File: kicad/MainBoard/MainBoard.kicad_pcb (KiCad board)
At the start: 2 copper layers, 191.5 x 166.3 mm, 104 parts, among them J1 CHAN1, J10 ACC Port, J11 433TX, J12 VDC INPUT, J13 BAT, J14 TRG1, J15 TRG2, J16 FP-BUTTONS, J17 EXPAN2, J18 OUTPUT_BOARD_POWER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

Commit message: Convert board to Kicad 8
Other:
- net class Default removed

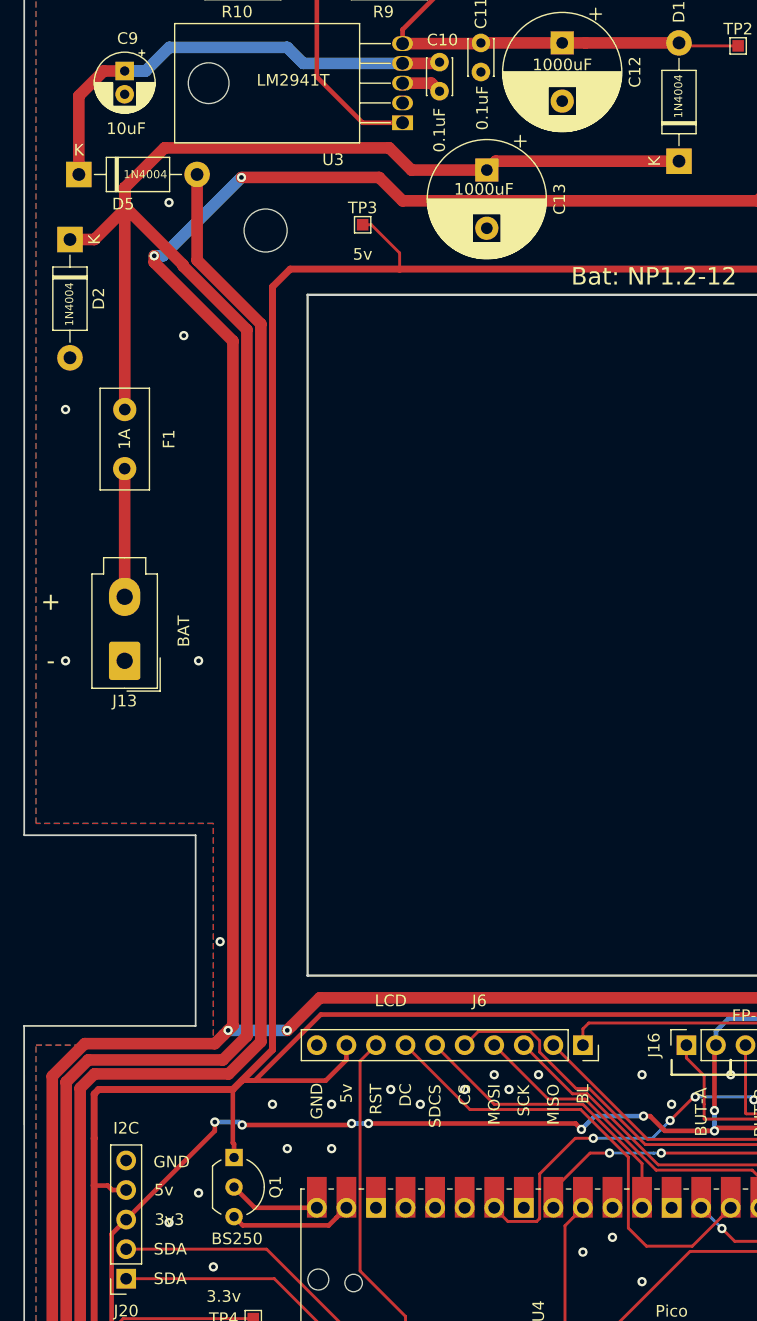
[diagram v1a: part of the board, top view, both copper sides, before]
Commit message: Switch Mainboard Q1, D1, D2, D5 with 1N5819
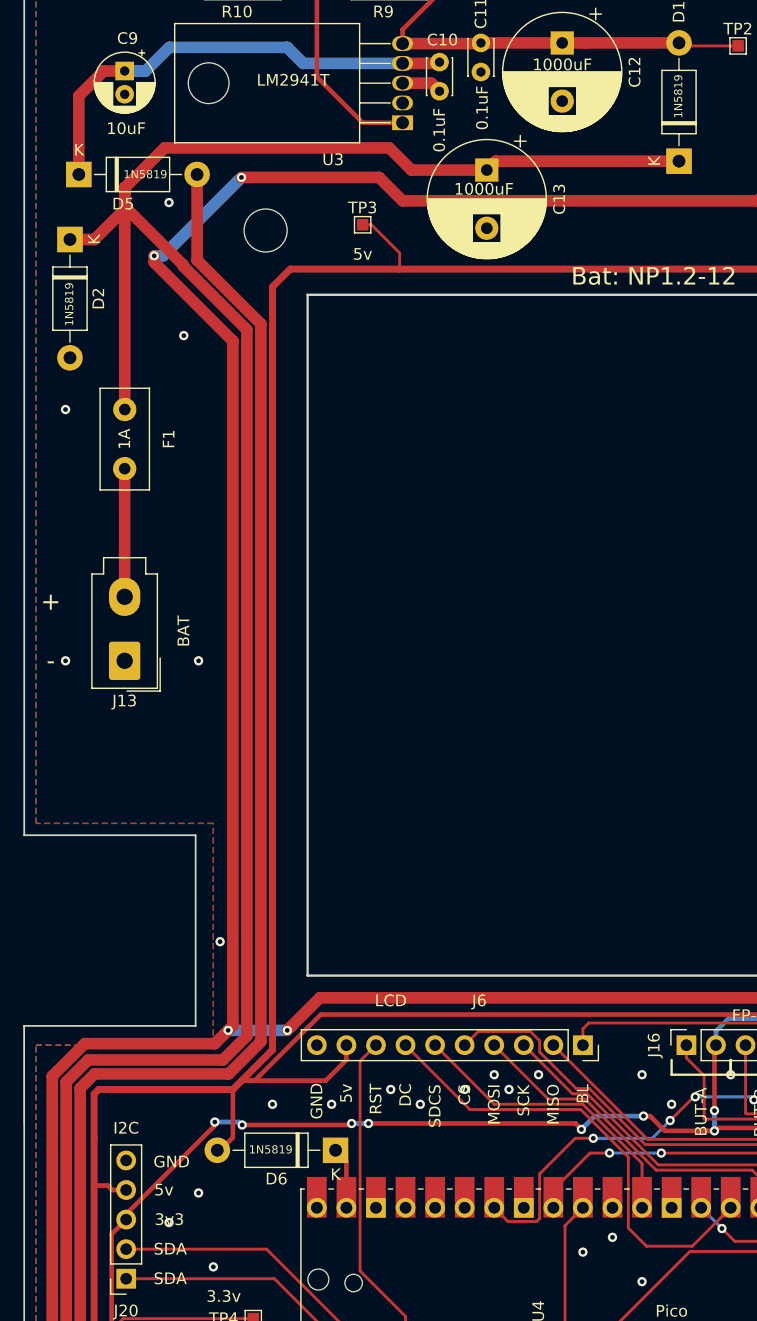
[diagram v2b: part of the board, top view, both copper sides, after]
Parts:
- removed Q1: BS250, Package_TO_SOT_THT:TO-92_Inline_Wide
- added D6: 1N5819, Diode_THT:D_DO-41_SOD81_P10.16mm_Horizontal, F.Cu at (42.2, 118.2)
- D1, D2, D5: value 1N4004 -> 1N5819
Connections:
- J1 pad R: (no net) -> unconnected-(J1-PadR)
- J10 pad 1: (no net) -> unconnected-(J10-Pad1)
- J14 pad RN: (no net) -> unconnected-(J14-PadRN)
- J14 pad TN: (no net) -> unconnected-(J14-PadTN)
- J15 pad RN: (no net) -> unconnected-(J15-PadRN)
- J15 pad TN: (no net) -> unconnected-(J15-PadTN)
- J18 pad 10: (no net) -> unconnected-(J18-Pin_10-Pad10)
- J18 pad 3: (no net) -> unconnected-(J18-Pin_3-Pad3)
- J18 pad 4: (no net) -> unconnected-(J18-Pin_4-Pad4)
- J18 pad 5: (no net) -> unconnected-(J18-Pin_5-Pad5)
- J18 pad 6: (no net) -> unconnected-(J18-Pin_6-Pad6)
- J18 pad 7: (no net) -> unconnected-(J18-Pin_7-Pad7)
- J18 pad 8: (no net) -> unconnected-(J18-Pin_8-Pad8)
- J18 pad 9: (no net) -> unconnected-(J18-Pin_9-Pad9)
- J2 pad R: (no net) -> unconnected-(J2-PadR)
- J4 pad 10: (no net) -> unconnected-(J4-Pin_10-Pad10)
- J4 pad 3: (no net) -> unconnected-(J4-Pin_3-Pad3)
- J4 pad 6: (no net) -> unconnected-(J4-Pin_6-Pad6)
- J4 pad 7: (no net) -> unconnected-(J4-Pin_7-Pad7)
- J5 pad R: (no net) -> unconnected-(J5-PadR)
- J7 pad R: (no net) -> unconnected-(J7-PadR)
- U4 pad 30: Net-(U4-Pad30) -> unconnected-(U4-RUN-Pad30)_0
- U4 pad 35: Net-(U4-Pad35) -> unconnected-(U4-ADC_VREF-Pad35)
- U4 pad 36: Net-(U4-Pad36) -> unconnected-(U4-3V3-Pad36)
- U4 pad 37: Net-(U4-Pad37) -> unconnected-(U4-3V3_EN-Pad37)
- U4 pad 40: Net-(Q1-Pad2) -> unconnected-(U4-VBUS-Pad40)_0
- U4 pad 41: Net-(U4-Pad41) -> unconnected-(U4-SWCLK-Pad41)
- U4 pad 42: Net-(U4-Pad42) -> unconnected-(U4-GND-Pad42)_0
- U4 pad 43: Net-(U4-Pad43) -> unconnected-(U4-SWDIO-Pad43)
- U8 pad 7: (no net) -> unconnected-(U8-P3-Pad7)
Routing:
- net Net-(Q1-Pad2): track 7.85 -> 0.00 mm
- net Net-(D6-K): track 10.6 -> 5.33 mm
- net GND: vias 100 -> 98

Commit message: Fix outline
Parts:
- moved D6 1.00 mm to (41.2, 118.2)
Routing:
- net 5v: track 571.2 -> 570.4 mm
- net 3v3: vias 28 -> 26
- net GND: vias 98 -> 100
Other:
- outline, holes or cut-outs redrawn
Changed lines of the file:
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@@
 	(footprint "Diode_THT:D_DO-41_SOD81_P10.16mm_Horizontal"
 		(layer "F.Cu")
-		(at 42.25 118.25 180)
+		(at 41.25 118.25 180)
 		(descr "Diode, DO-41_SOD81 series, Axial, Horizontal, pin pitch=10.16mm, , length*diameter=5.2*2.7mm^2, , http://www.diodes.com/_files/packages/DO-41%20(Plastic).pdf")
 		(tags "Diode DO-41_SOD81 series Axial Horizontal pin pitch 10.16mm  length 5.2mm diameter 2.7mm")
@@
 			(layer "F.Fab")
 		)
-		(fp_text user "K"
-			(at 0 -2.1 180)
-			(layer "F.SilkS")
-			(effects
-				(font
-					(size 1 1)
-					(thickness 0.15)
-				)
-			)
-		)
 		(fp_text user "${REFERENCE}"
 			(at 5.47 0 180)
@@
 			)
 		)
-		(fp_text user "K"
-			(at 0 -2.1 180)
-			(layer "F.Fab")
-			(effects
-				(font
-					(size 1 1)
-					(thickness 0.15)
-				)
-			)
-		)
 		(pad "1" thru_hole rect
 			(at 0 0 180)
@@
 	(gr_line
 		(start 39.849 44.753)
-		(end 39.849 103.253)
+		(end 39.839 103.243)
 		(stroke
 			(width 0.2)
@@
 	(gr_line
 		(start 15.500364 16.150548)
-		(end 206.980364 16.150548)
+		(end 206.983141 16.153779)
 		(stroke
 			(width 0.15)
@@
 	)
 	(gr_line
-		(start 206.963141 91.153779)
+		(start 206.983141 91.153779)
 		(end 191.983141 91.153779)
 		(stroke
@@
 	)
 	(gr_line
-		(start 140.849 44.753)
-		(end 140.849 103.253)
+		(start 140.849 44.75)
+		(end 140.839 103.243)
 		(stroke
 			(width 0.2)
@@
 	)
 	(gr_line
-		(start 15.494 91.186)
-		(end 30.226 91.186)
+		(start 15.5 91.15)
+		(end 30.232 91.15)
 		(stroke
 			(width 0.15)
@@
 	)
 	(gr_line
-		(start 15.494 107.569)
-		(end 30.226 107.569)
+		(start 15.494364 107.569548)
+		(end 30.232 107.533)
 		(stroke
 			(width 0.15)
@@
 	)
 	(gr_line
-		(start 30.226 91.186)
-		(end 30.226 107.569)
+		(start 30.232 91.15)
+		(end 30.232 107.533)
 		(stroke
 			(width 0.15)
@@
 	)
 	(gr_line
-		(start 15.5 182.45)
-		(end 15.494 107.569)
+		(start 15.500364 182.450548)
+		(end 15.494364 107.569548)
 		(stroke
 			(width 0.15)
@@
 	)
 	(segment
+		(start 39.299 115.951)
+		(end 43.630001 115.951)
+		(width 0.4)
+		(layer "F.Cu")
+		(net 1)
+	)
+	(segment
 		(start 23.114 133.604)
 		(end 23.006999 133.604)
@@
 	)
 	(segment
-		(start 34.22315 116.078)
-		(end 43.503001 116.078)
-		(width 0.4)
-		(layer "F.Cu")
-		(net 1)
-	)
-	(segment
 		(start 137.668 131.699)
 		(end 146.812 131.699)
@@
 	)
 	(segment
+		(start 24.257 124.206)
+		(end 31.044 124.206)
+		(width 0.4)
+		(layer "F.Cu")
+		(net 1)
+	)
+	(segment
 		(start 167.005 146.939)
 		(end 167.005 129.794)
@@
 	)
 	(segment
-		(start 24.257 123.743)
-		(end 31.877 116.123)
-		(width 0.4)
-		(layer "F.Cu")
-		(net 1)
-	)
-	(segment
 		(start 23.006999 135.617999)
 		(end 24.257 136.868)
@@
 	)
 	(segment
-		(start 31.877 116.123)
-		(end 31.877 115.824)
-		(width 0.4)
-		(layer "F.Cu")
-		(net 1)
-	)
-	(segment
 		(start 146.812 131.699)
 		(end 148.59 133.477)
@@
 	)
 	(segment
+		(start 31.044 124.206)
+		(end 39.299 115.951)
+		(width 0.4)
+		(layer "F.Cu")
+		(net 1)
+	)
+	(segment
 		(start 61.359999 151.402999)
 		(end 61.359999 152.164999)
@@
 	)
 	(via
-		(at 34.22315 116.078)
-		(size 0.8)
-		(drill 0.4)
-		(layers "F.Cu" "B.Cu")
-		(net 1)
-	)
-	(via
-		(at 31.877 115.824)
-		(size 0.8)
-		(drill 0.4)
-		(layers "F.Cu" "B.Cu")
-		(net 1)
-	)
-	(via
 		(at 173.863 60.96)
 		(size 0.8)
@@
 	)
 	(segment
-		(start 33.96915 115.824)
-		(end 34.22315 116.078)
-		(width 0.4)
-		(layer "B.Cu")
-		(net 1)
-	)
-	(segment
 		(start 43.630001 115.951)
 		(end 45.080001 115.951)
@@
 	)
 	(segment
-		(start 31.877 115.824)
-		(end 33.96915 115.824)
-		(width 0.4)
-		(layer "B.Cu")
-		(net 1)
-	)
-	(segment
 		(start 85.09 109.22)
 		(end 85.09 108.017919)
@@
 	)
 	(via
+		(at 51.5 127.75)
+		(size 0.8)
+		(drill 0.4)
+		(layers "F.Cu" "B.Cu")
+		(net 2)
+	)
+	(via
 		(at 66.04 125.73)
 		(size 0.8)
@@
 	)
 	(via
-		(at 27.94 124.46)
+		(at 30.5 121.5)
 		(size 0.8)
 		(drill 0.4)
@@
 	)
 	(via
+		(at 25.75 116)
+		(size 0.8)
+		(drill 0.4)
+		(layers "F.Cu" "B.Cu")
+		(net 2)
+	)
+	(via
 		(at 19.05 76.2)
 		(size 0.8)
@@
 	)
 	(via
-		(at 30.48 121.92)
+		(at 35.25 124.5)
 		(size 0.8)
 		(drill 0.4)
@@
 	)
 	(segment
+		(start 31.09 113.12)
+		(end 31 113.03)
+		(width 0.4)
+		(layer "F.Cu")
+		(net 9)
+	)
+	(segment
 		(start 56.007 164.592)
 		(end 56.007 164.465)
@@
 	)
 	(segment
-		(start 33.42315 117.16685)
-		(end 33.42315 113.03)
-		(width 0.4)
-		(layer "F.Cu")
-		(net 9)
-	)
-	(segment
 		(start 21.50703 121.285)
 		(end 21.50703 136.525)
@@
 	)
 	(segment
+		(start 31.09 118.25)
+		(end 31.09 113.12)
+		(width 0.4)
+		(layer "F.Cu")
+		(net 9)
+	)
+	(segment
 		(start 45.085 174.125002)
 		(end 47.235998 176.276)
@@
 	)
 	(segment
+		(start 31 113.03)
+		(end 21.89007 113.03)
+		(width 0.6)
+		(layer "F.Cu")
+		(net 9)
+	)
+	(segment
 		(start 112.903 19.812)
 		(end 112.903 30.4)
@@
 	)
 	(segment
-		(start 33.42315 113.03)
-		(end 21.89007 113.03)
-		(width 0.6)
-		(layer "F.Cu")
-		(net 9)
-	)
-	(segment
 		(start 40.98401 106.58999)
 		(end 108.019315 106.58999)
@@
 	)
 	(segment
-		(start 32.09 118.5)
-		(end 33.42315 117.16685)
-		(width 0.4)
-		(layer "F.Cu")
-		(net 9)
-	)
-	(segment
 		(start 43.18 110.49)
 		(end 43.18 109.22)
@@
 	)
 	(segment
+		(start 33.42315 113.03)
+		(end 31 113.03)
+		(width 0.6)
+		(layer "F.Cu")
+		(net 9)
+	)
+	(segment
 		(start 121.412 32.766)
 		(end 121.412 30.734)
@@
 	)
 	(segment
-		(start 43.18 119.18)
-		(end 42.25 118.25)
+		(start 43.18 123.19)
+		(end 43.18 120.18)
 		(width 0.4)
 		(layer "F.Cu")
@@
 	)
 	(segment
-		(start 43.18 123.19)
-		(end 43.18 119.18)
+		(start 43.18 120.18)
+		(end 41.25 118.25)
 		(width 0.4)
 		(layer "F.Cu")

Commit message: Move things a bit for potential additional header
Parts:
- moved C5 4.40 mm to (110.4, 162.5)
- moved C3 4.40 mm to (105.6, 160.3)
- moved C4 4.40 mm to (113.2, 160.3)
- moved C6 4.40 mm to (118.3, 162.5)
- moved J8 4.40 mm to (104.2, 143.8)
- moved C1 4.40 mm to (98.5, 147.2)
- moved U2 4.40 mm to (105.6, 156.7)
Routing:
- net Net-(J8-Pin_2): track 68.4 -> 73.1 mm
- net 3v3: track 527.3 -> 531.3 mm
- net MCU-UART0-RX: track 86.7 -> 90.7 mm
- net 232-TX: track 25.6 -> 29.7 mm
- net Net-(J8-Pin_6): track 75.3 -> 79.3 mm
- net Net-(J8-Pin_4): track 68.5 -> 72.6 mm
- net 232-RX: track 24.3 -> 28.3 mm
- net Net-(J8-Pin_5): track 77.8 -> 81.9 mm
- net MCU-UART0-TX: track 83.2 -> 87.2 mm
- net MCU-UART1-RX: track 61.7 -> 65.0 mm
- net MCU-UART1-TX: track 61.2 -> 64.3 mm
- net GND: vias 100 -> 108

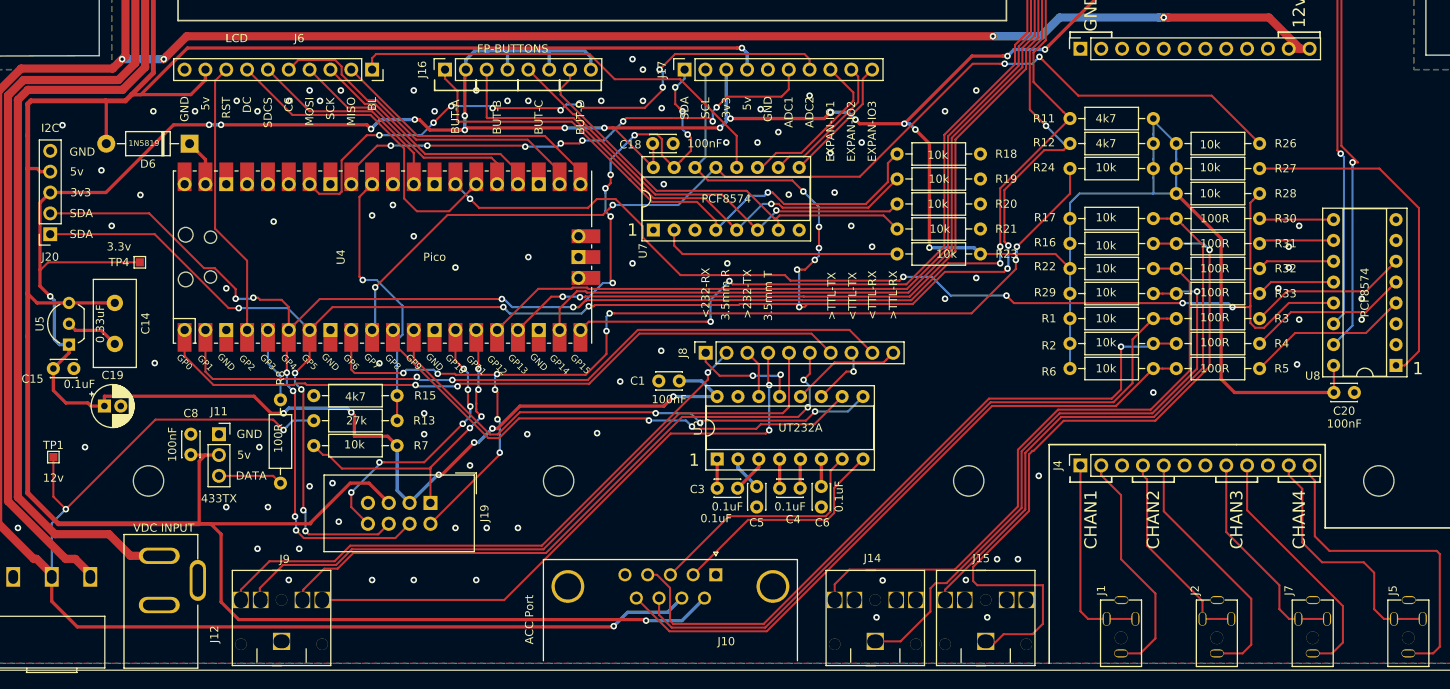
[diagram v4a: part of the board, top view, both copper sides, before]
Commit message: Add header for RS232 configuration
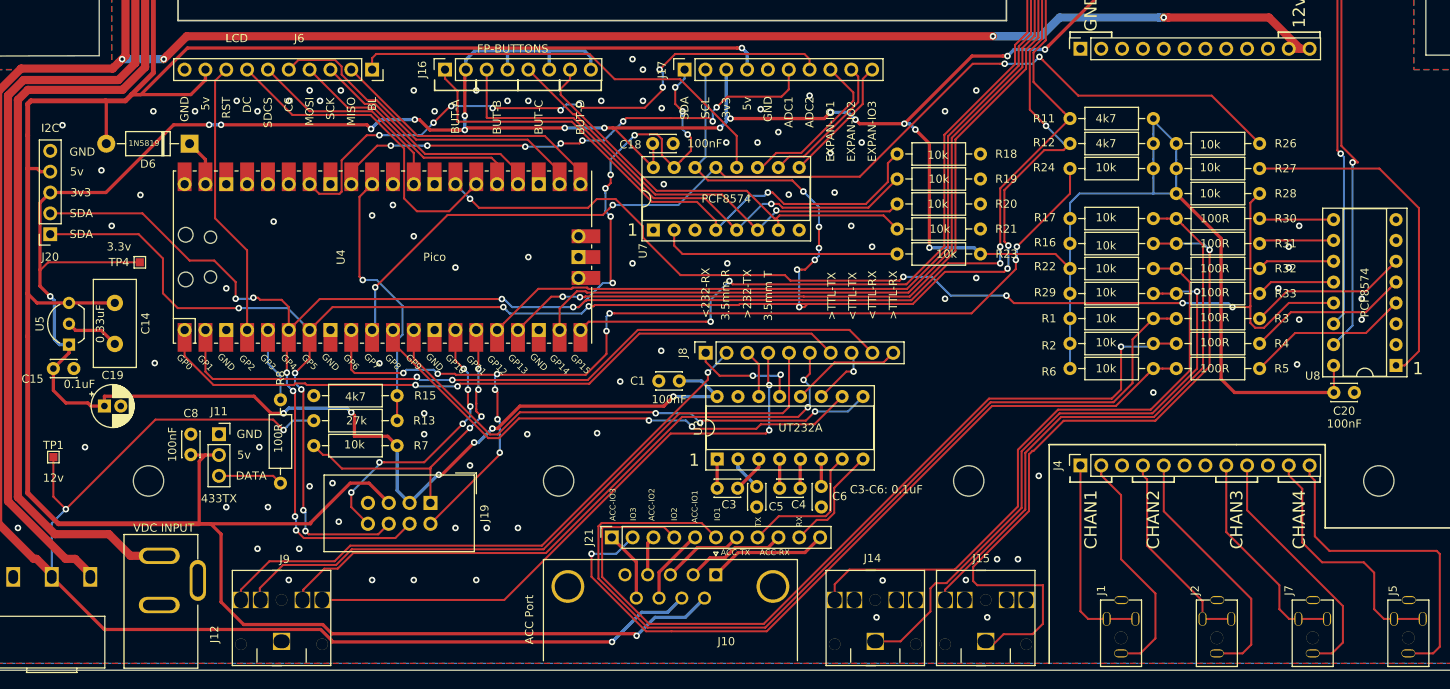
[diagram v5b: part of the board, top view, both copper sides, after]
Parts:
- added J21: EXPAN3, Connector_PinSocket_2.54mm:PinSocket_1x11_P2.54mm_Vertical, F.Cu at (92.7, 166.2)
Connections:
- J10 pad 1: unconnected-(J10-Pad1) -> ACCP-PIN1
- J10 pad 2: 232-RX -> ACCP-232-RX
- J10 pad 3: 232-TX -> ACCP-232-TX
- J10 pad 4: Net-(J10-Pad4) -> ACCP-IO-2
- J10 pad 8: Net-(J10-Pad8) -> ACCP-IO-3
- J10 pad 9: Net-(J10-Pad9) -> ACCP-IO-1
- R1 pad 2: Net-(J10-Pad8) -> Net-(J21-Pin_6)
- R2 pad 2: Net-(J10-Pad4) -> Net-(J21-Pin_4)
- R3 pad 2: Net-(J10-Pad8) -> Net-(J21-Pin_6)
- R4 pad 2: Net-(J10-Pad4) -> Net-(J21-Pin_4)
- R5 pad 2: Net-(J10-Pad9) -> Net-(J21-Pin_2)
- R6 pad 2: Net-(J10-Pad9) -> Net-(J21-Pin_2)
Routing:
- net Net-(J21-Pin_6): track 0.00 -> 113.2 mm
- net Net-(J21-Pin_4): track 0.00 -> 104.9 mm, vias 0 -> 1
- net Net-(J21-Pin_2): track 0.00 -> 96.0 mm, vias 0 -> 1
- net Net-(J10-Pad4): track 86.5 -> 0.00 mm, vias 1 -> 0
- net Net-(J10-Pad8): track 84.5 -> 0.00 mm
- net Net-(J10-Pad9): track 80.8 -> 0.00 mm
- net 232-RX: track 28.3 -> 13.5 mm
- net ACCP-PIN1: track 0.00 -> 14.6 mm
- net ACCP-232-RX: track 0.00 -> 12.8 mm
- net 232-TX: track 29.7 -> 17.2 mm
- net ACCP-232-TX: track 0.00 -> 9.98 mm
- net ACCP-IO-3: track 0.00 -> 9.31 mm
- net ACCP-IO-1: track 0.00 -> 8.65 mm
- net ACCP-IO-2: track 0.00 -> 4.85 mm
- net SCL: track 400.4 -> 402.9 mm
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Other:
- board text added: "ACC-IO1"
- board text added: "ACC-IO2"
- board text added: "ACC-IO3"
- board text added: "ACC-RX"
- board text added: "ACC-TX"
- board text added: "C3-C6: 0.1uF"
- board text added: "IO1"
- board text added: "IO2"
- board text added: "IO3"
- board text added: "RX"
- board text added: "TX"

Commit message: Before 3.5mm footprint switch
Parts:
- J1, J5, J7: footprint ProjLib:PJ-2100B-4A -> ProjLib:PJ-3062-CO
- J2: value CHAN2 -> CHAN1; footprint ProjLib:PJ-2100B-4A -> ProjLib:PJ-3062-CO
- moved J5 11.8 mm to (196.9, 183.0), turned to 180 degrees
- moved J7 10.4 mm to (183.7, 183.0), turned to 180 degrees
- moved J2 9.20 mm to (170.4, 183.0), turned to 180 degrees
- moved J1 7.89 mm to (156.9, 183.0), turned to 180 degrees
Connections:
- J1 pad R: unconnected-(J1-PadR) -> Net-(J4-Pin_1)
- J2 pad R: unconnected-(J2-PadR) -> Net-(J4-Pin_4)
- J5 pad R: unconnected-(J5-PadR) -> Net-(J4-Pin_11)
- J7 pad R: unconnected-(J7-PadR) -> Net-(J4-Pin_8)
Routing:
- net Net-(J4-Pin_2): track 28.8 -> 0.00 mm
- net Net-(J4-Pin_5): track 30.9 -> 5.59 mm
- net Net-(J4-Pin_4): track 25.2 -> 0.00 mm
- net Net-(J4-Pin_8): track 26.5 -> 17.3 mm
- net Net-(J4-Pin_9): track 30.7 -> 22.0 mm
- net Net-(J4-Pin_1): track 24.9 -> 28.7 mm
